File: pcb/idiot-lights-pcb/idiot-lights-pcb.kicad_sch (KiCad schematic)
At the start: 25 parts, among them SW1 Toggle left indicator, SW2 Toggle right indicator, SW3 Toggle hazard warning, SW4 Break control, SW5 Reset

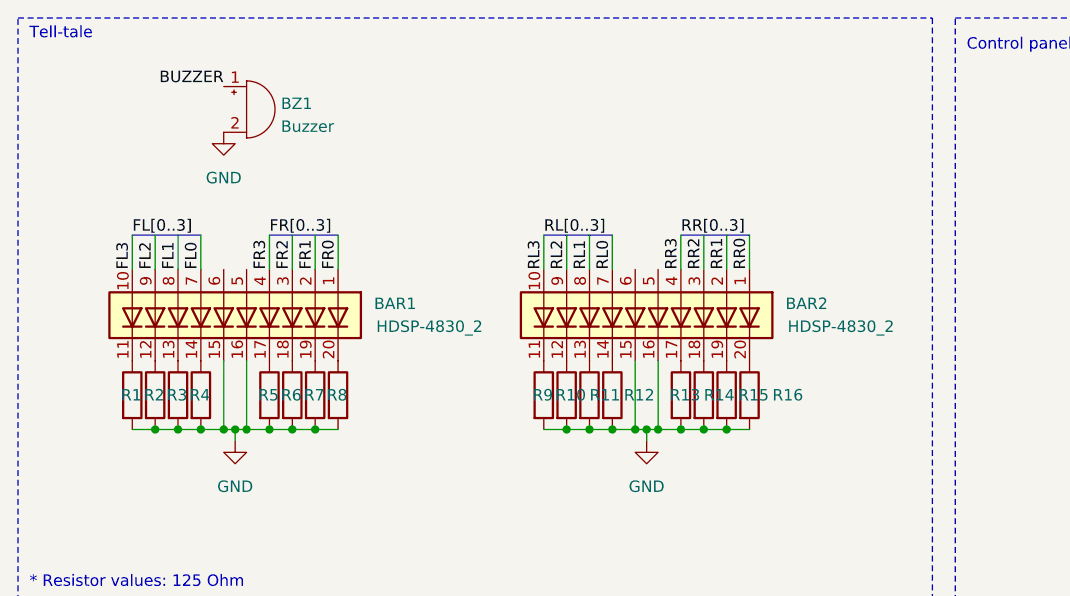
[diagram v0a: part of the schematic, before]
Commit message: Switch from THT to SMD for multiple components
Buzzer & LED lights arrays
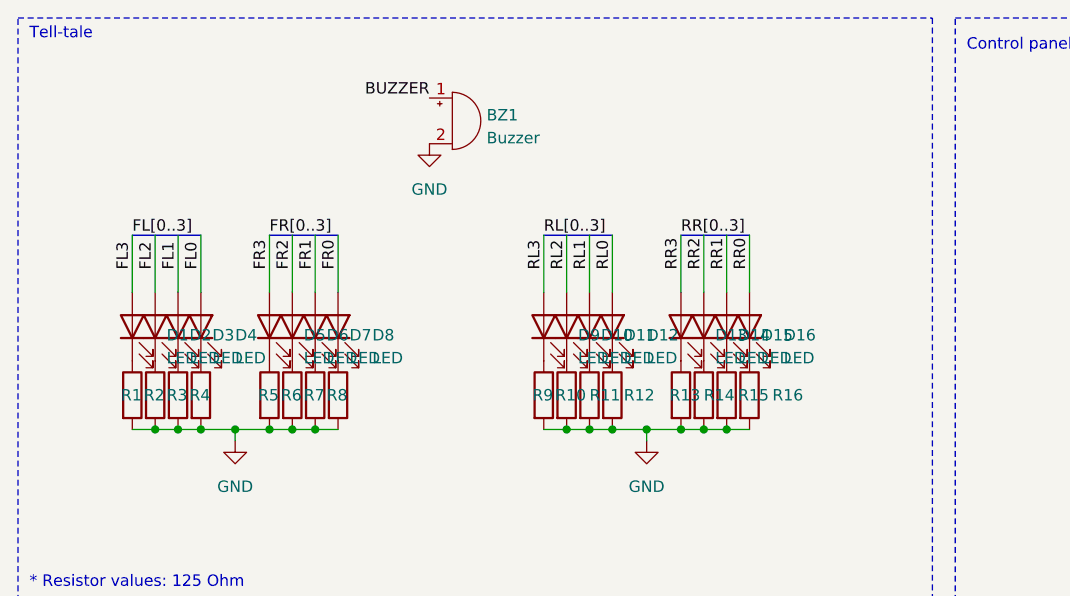
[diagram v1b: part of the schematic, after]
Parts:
- removed BAR1, BAR2: HDSP-4830_2, Display:HDSP-4830, symbol LED:HDSP-4830_2
- added D1, D10, D11, D12, D13, D14, D15, D16, D2, D3, D4, D5, D6, D7, D8, D9: LED, LED_SMD_no_silk:LED_0603_1608Metric_no_silk, symbol Device:LED
- BZ1: footprint Buzzer_Beeper:Buzzer_12x9.5RM7.6 -> Buzzer_Beeper:PUIAudio_SMT_0825_S_4_R
- SW1, SW2, SW3, SW4, SW5: footprint Button_Switch_THT:SW_PUSH_6mm_H5mm -> Button_Switch_SMD:SW_SPST_PTS645
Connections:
- net FL0: now also D4.2 (A)
- net FL1: now also D3.2 (A)
- net FL2: now also D2.2 (A)
- net FL3: now also D1.2 (A)
- net FR0: now also D8.2 (A)
- net FR1: now also D7.2 (A)
- net FR2: now also D6.2 (A)
- net FR3: now also D5.2 (A)
- net RL0: now also D12.2 (A)
- net RL1: now also D11.2 (A)
- net RL2: now also D10.2 (A)
- net RL3: now also D9.2 (A)
- net RR0: now also D13.2 (A), D16.2 (A)
- net RR1: now also D15.2 (A)
- net RR2: now also D14.2 (A)
- net at R8.1: now also D8.1 (K)
- net at R4.1: now also D4.1 (K)
- net at R12.1: now also D12.1 (K)
- net at R13.1: now also D13.1 (K)
- net at R3.1: now also D3.1 (K)
- net at R1.1: now also D1.1 (K)
- net at R9.1: now also D9.1 (K)
- net at R2.1: now also D2.1 (K)
- net at R5.1: now also D5.1 (K)
- net at R6.1: now also D6.1 (K)
- net at R7.1: now also D7.1 (K)
- net at R15.1: now also D15.1 (K)
- net at R10.1: now also D10.1 (K)
- net at R11.1: now also D11.1 (K)
- net at R14.1: now also D14.1 (K)
- net at R16.1: now also D16.1 (K)
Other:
- moved on the sheet: BZ1
